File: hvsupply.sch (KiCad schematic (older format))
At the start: 30 parts, among them Q1 TIP50, Q2 IRF740, Q3 IRF740, Q4 IRF740, U1 LR8

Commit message: Beginning to look like a PCB.
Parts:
- removed C?: 1u, ~, symbol C
- removed K?: CONN_3, symbol CONN_3
- removed P?: CONN_2, symbol CONN_2
- added C3, C4, C5, C6, C7: .01, ~, symbol C
- added D5, D6: 16V, 1.3W, ~, symbol ZENER
- added K1: CONN_3, symbol CONN_3
- added P1, P2, P3, P4: CONN_2, symbol CONN_2
- added P10, P5, P6, P7, P8, P9: CONN_1, symbol CONN_1
- added Q2, Q3: IRF740, TO220, symbol IRF740
- added R10, R11: 16.2, 3W, ~, symbol R
- added R15: 10M, ~, symbol R
- added R16: 10k, ~, symbol R
- added R5, R6: 100, ~, symbol R
- gave numbers to parts that had none: 3
- renumbered D5 to D7, D6 to D8, D7 to D9, Q2 to Q4, Q3 to Q5, Q4 to Q6, R7 to R12, R8 to R13, R9 to R14, R1 to R2, R2 to R3, R3 to R4, R4 to R7, R5 to R8, R6 to R9
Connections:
- net GND: now also C3.1, C4.1, C5.1, C6.1, C7.1, P1.2 (PM), P10.1, P3.2 (PM), P4.2 (PM), P5.1, P6.1, P7.1, P8.1, P9.1, R16.2
- net HV_UNREG: now reaches C1.1, C2.1, D2.2 (K), D4.2 (K), Q4.1 (D), Q5.1 (D), Q6.1 (D), U1.1 (VIN)
- net HV_UNREG: now also Q2.1 (D), Q3.1 (D)
- net at D7.2 (K), Q4.2 (G), R7.2: now also C5.2
- net at D8.2 (K), Q5.2 (G), R8.2: now also C6.2
- net at D9.2 (K), Q6.2 (G), R9.2: now also C7.2
- net at R7.1, R8.1, R9.1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: now also R2.1, R5.1, R6.1
- net HV_OUT: now reaches R12.2, R13.2, R14.2
- net HV_OUT: now also P2.1 (P1), R10.2, R11.2, R15.1
- net SENSE_I: now reaches Q1.1 (B), R3.2, R4.1
- net SENSE_I: now also P2.2 (PM), P3.1 (P1)
- net HV_IN_LO: now reaches K2.1 (T1)
- net HV_IN_LO: now also K1.3 (P3)
- net HV_IN_HI: now reaches K2.14 (R2), K2.16 (T2)
- net HV_IN_HI: now also K1.1 (P1)
- net at K2.3 (R1): now also K1.2 (PM)
- net +12V renamed 12V_IN
- net 12V_IN: now also P1.1 (P1)
- new net: C4.2, D6.2 (K), Q3.2 (G), R6.2
- new net: D6.1 (A), Q3.3 (S), R11.1
- new net: C3.2, D5.2 (K), Q2.2 (G), R5.2
- new net: D5.1 (A), Q2.3 (S), R10.1
- new net SENSE_V: P4.1 (P1), R15.2, R16.1
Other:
- moved on the sheet: C1, C2, D1, D2, D3, D4, D7, D8, D9, K2, Q1, Q4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

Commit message: Fixed circuit error, added VCR for current limit adjustment, prototyping current limit indicator.
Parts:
- removed R4: 2.37, ~, symbol R
- added D?: LED, ~, symbol LED
- added Q?: MOSFET_N, ~, symbol MOSFET_N
- added Q?: PNP, ~, symbol PNP
- added R? (x3): R, ~, symbol R
- added RV?: POT, ~, symbol POT
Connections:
- net GND: now also Q?.S, R?.2, R?.2
- net SENSE_I: now also Q?.D, R?.1
- net at Q1.2 (C), U1.3 (ADJ): now also R2.2, RV1.2, RV1.3, Q?.2 (B)
- new net: Q?.G, R?.1, R?.2, RV?.3
- new net: D?.1 (A), Q?.3 (C)
- new net: D?.2 (K), R?.1
- new net +12V: Q?.1 (E), RV?.1, RV?.2
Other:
- note added: "Current Limit Indicator"
- note added: "Current Limit VCR"
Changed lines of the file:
@@
-EESchema Schematic File Version 2  date 7/6/2013 6:08:41 PM
+EESchema Schematic File Version 2  date 7/12/2013 8:46:22 PM
 LIBS:power
 LIBS:device
@@
 Sheet 1 1
 Title "Adjustable High Voltage Bench Supply"
-Date "7 jul 2013"
+Date "12 jul 2013"
 Rev ""
 Comp ""
@@
 $EndComp
 $Comp
-L R R4
-U 1 1 518B207E
-P 6350 5750
-F 0 "R4" V 6430 5750 40  0000 C CNN
-F 1 "2.37" V 6357 5751 40  0000 C CNN
-F 2 "~" V 6280 5750 30  0000 C CNN
-F 3 "~" H 6350 5750 30  0000 C CNN
-	1    6350 5750
-	1    0    0    -1
-$EndComp
-$Comp
 L CP1 C1
 U 1 1 518B20BA
@@
 F 3 "" H 4700 4550 60  0000 C CNN
 	1    4700 4550
-	1    0    0    -1
-$EndComp
-$Comp
-L GND #PWR03
-U 1 1 518B2146
-P 6350 6050
-F 0 "#PWR03" H 6350 6050 30  0001 C CNN
-F 1 "GND" H 6350 5980 30  0001 C CNN
-F 2 "" H 6350 6050 60  0000 C CNN
-F 3 "" H 6350 6050 60  0000 C CNN
-	1    6350 6050
 	1    0    0    -1
 $EndComp
@@
 	5000 2800 7850 2800
 Wire Wire Line
-	6350 5450 6350 5500
+	6350 5450 6350 6050
 Wire Wire Line
 	5900 5500 8600 5500
@@
 	3950 4350 3900 4350
 Connection ~ 3900 4350
-Wire Wire Line
-	6350 6000 6350 6050
 Wire Wire Line
 	7100 3350 7100 3400
@@
 Text Label 6750 2800 2    60   ~ 0
 HV_UNREG
+$Comp
+L MOSFET_N Q?
+U 1 1 51E03006
+P 6450 6250
+F 0 "Q?" H 6460 6420 60  0000 R CNN
+F 1 "MOSFET_N" H 6460 6100 60  0000 R CNN
+F 2 "~" H 6450 6250 60  0000 C CNN
+F 3 "~" H 6450 6250 60  0000 C CNN
+	1    6450 6250
+	-1   0    0    -1
+$EndComp
+$Comp
+L POT RV?
+U 1 1 51E0301C
+P 7250 6250
+F 0 "RV?" H 7250 6150 50  0000 C CNN
+F 1 "POT" H 7250 6250 50  0000 C CNN
+F 2 "~" H 7250 6250 60  0000 C CNN
+F 3 "~" H 7250 6250 60  0000 C CNN
+	1    7250 6250
+	-1   0    0    -1
+$EndComp
+$Comp
+L R R?
+U 1 1 51E03032
+P 6750 5900
+F 0 "R?" V 6830 5900 40  0000 C CNN
+F 1 "R" V 6757 5901 40  0000 C CNN
+F 2 "~" V 6680 5900 30  0000 C CNN
+F 3 "~" H 6750 5900 30  0000 C CNN
+	1    6750 5900
+	0    -1   -1   0
+$EndComp
+$Comp
+L R R?
+U 1 1 51E03041
+P 7000 6750
+F 0 "R?" V 7080 6750 40  0000 C CNN
+F 1 "R" V 7007 6751 40  0000 C CNN
+F 2 "~" V 6930 6750 30  0000 C CNN
+F 3 "~" H 7000 6750 30  0000 C CNN
+	1    7000 6750
+	1    0    0    -1
+$EndComp
+$Comp
+L PNP Q?
+U 1 1 51E03050
+P 5000 5200
+F 0 "Q?" H 5000 5050 60  0000 R CNN
+F 1 "PNP" H 5000 5350 60  0000 R CNN
+F 2 "~" H 5000 5200 60  0000 C CNN
+F 3 "~" H 5000 5200 60  0000 C CNN
+	1    5000 5200
+	-1   0    0    1
+$EndComp
+$Comp
+L LED D?
+U 1 1 51E03064
+P 4900 5800
+F 0 "D?" H 4900 5900 50  0000 C CNN
+F 1 "LED" H 4900 5700 50  0000 C CNN
+F 2 "~" H 4900 5800 60  0000 C CNN
+F 3 "~" H 4900 5800 60  0000 C CNN
+	1    4900 5800
+	0    1    1    0
+$EndComp
+$Comp
+L R R?
+U 1 1 51E03073
+P 4900 6350
+F 0 "R?" V 4980 6350 40  0000 C CNN
+F 1 "R" V 4907 6351 40  0000 C CNN
+F 2 "~" V 4830 6350 30  0000 C CNN
+F 3 "~" H 4900 6350 30  0000 C CNN
+	1    4900 6350
+	1    0    0    -1
+$EndComp
+$Comp
+L GND #PWR?
+U 1 1 51E03082
+P 4900 6800
+F 0 "#PWR?" H 4900 6800 30  0001 C CNN
+F 1 "GND" H 4900 6730 30  0001 C CNN
+F 2 "" H 4900 6800 60  0000 C CNN
+F 3 "" H 4900 6800 60  0000 C CNN
+	1    4900 6800
+	1    0    0    -1
+$EndComp
+$Comp
+L GND #PWR?
+U 1 1 51E03091
+P 6350 6700
+F 0 "#PWR?" H 6350 6700 30  0001 C CNN
+F 1 "GND" H 6350 6630 30  0001 C CNN
+F 2 "" H 6350 6700 60  0000 C CNN
+F 3 "" H 6350 6700 60  0000 C CNN
+	1    6350 6700
+	1    0    0    -1
+$EndComp
+$Comp
+L GND #PWR?
+U 1 1 51E030A0
+P 7000 7200
+F 0 "#PWR?" H 7000 7200 30  0001 C CNN
+F 1 "GND" H 7000 7130 30  0001 C CNN
+F 2 "" H 7000 7200 60  0000 C CNN
+F 3 "" H 7000 7200 60  0000 C CNN
+	1    7000 7200
+	1    0    0    -1
+$EndComp
+$Comp
+L +12V #PWR?
+U 1 1 51E030AF
+P 4900 4900
+F 0 "#PWR?" H 4900 4850 20  0001 C CNN
+F 1 "+12V" H 4900 5000 30  0000 C CNN
+F 2 "" H 4900 4900 60  0000 C CNN
+F 3 "" H 4900 4900 60  0000 C CNN
+	1    4900 4900
+	1    0    0    -1
+$EndComp
+Wire Wire Line
+	4900 4900 4900 5000
+Wire Wire Line
+	5200 5200 5600 5200
+Connection ~ 5600 5200
+Wire Wire Line
+	4900 5400 4900 5600
+Wire Wire Line
+	4900 6000 4900 6100
+Wire Wire Line
+	4900 6600 4900 6800
+Wire Wire Line
+	6350 5900 6500 5900
+Connection ~ 6350 5900
+Wire Wire Line
+	7000 5900 7000 6500
+Connection ~ 7000 6250
+Wire Wire Line
+	6650 6250 7000 6250
+Wire Wire Line
+	7250 6100 7500 6100
+Wire Wire Line
+	7500 5950 7500 6250
+$Comp
+L +12V #PWR?
+U 1 1 51E035F9
+P 7500 5950
+F 0 "#PWR?" H 7500 5900 20  0001 C CNN
+F 1 "+12V" H 7500 6050 30  0000 C CNN
+F 2 "" H 7500 5950 60  0000 C CNN
+F 3 "" H 7500 5950 60  0000 C CNN
+	1    7500 5950
+	1    0    0    -1
+$EndComp
+Connection ~ 7500 6100
+Wire Wire Line
+	7000 7000 7000 7200
+Wire Wire Line
+	6350 6450 6350 6700
+Text Notes 4700 6400 1    60   ~ 0
+Current Limit Indicator
+Text Notes 6250 6650 1    60   ~ 0
+Current Limit VCR
+Wire Wire Line
+	5600 4350 6350 4350
 $EndSCHEMATC

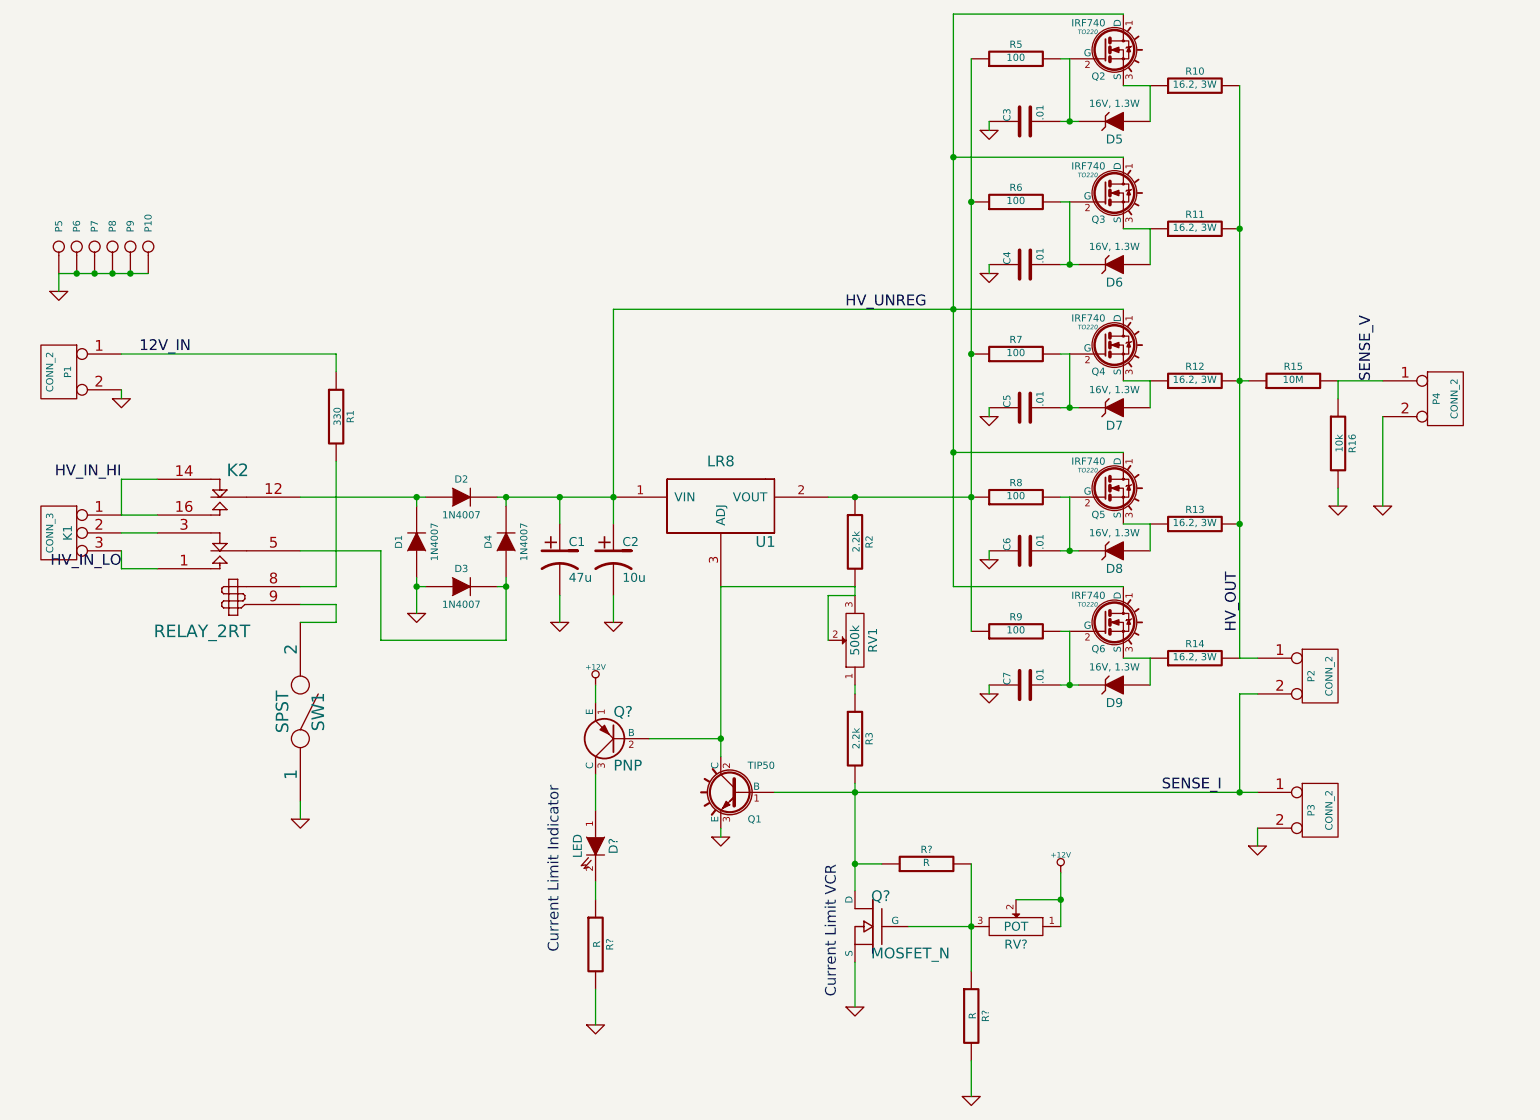
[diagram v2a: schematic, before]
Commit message: Major changes: unity-gain op-amps for current limit triggering and current sense buffering; comparator-based current limit indicator; voltage-controlled resistor-based adjustable current limit.
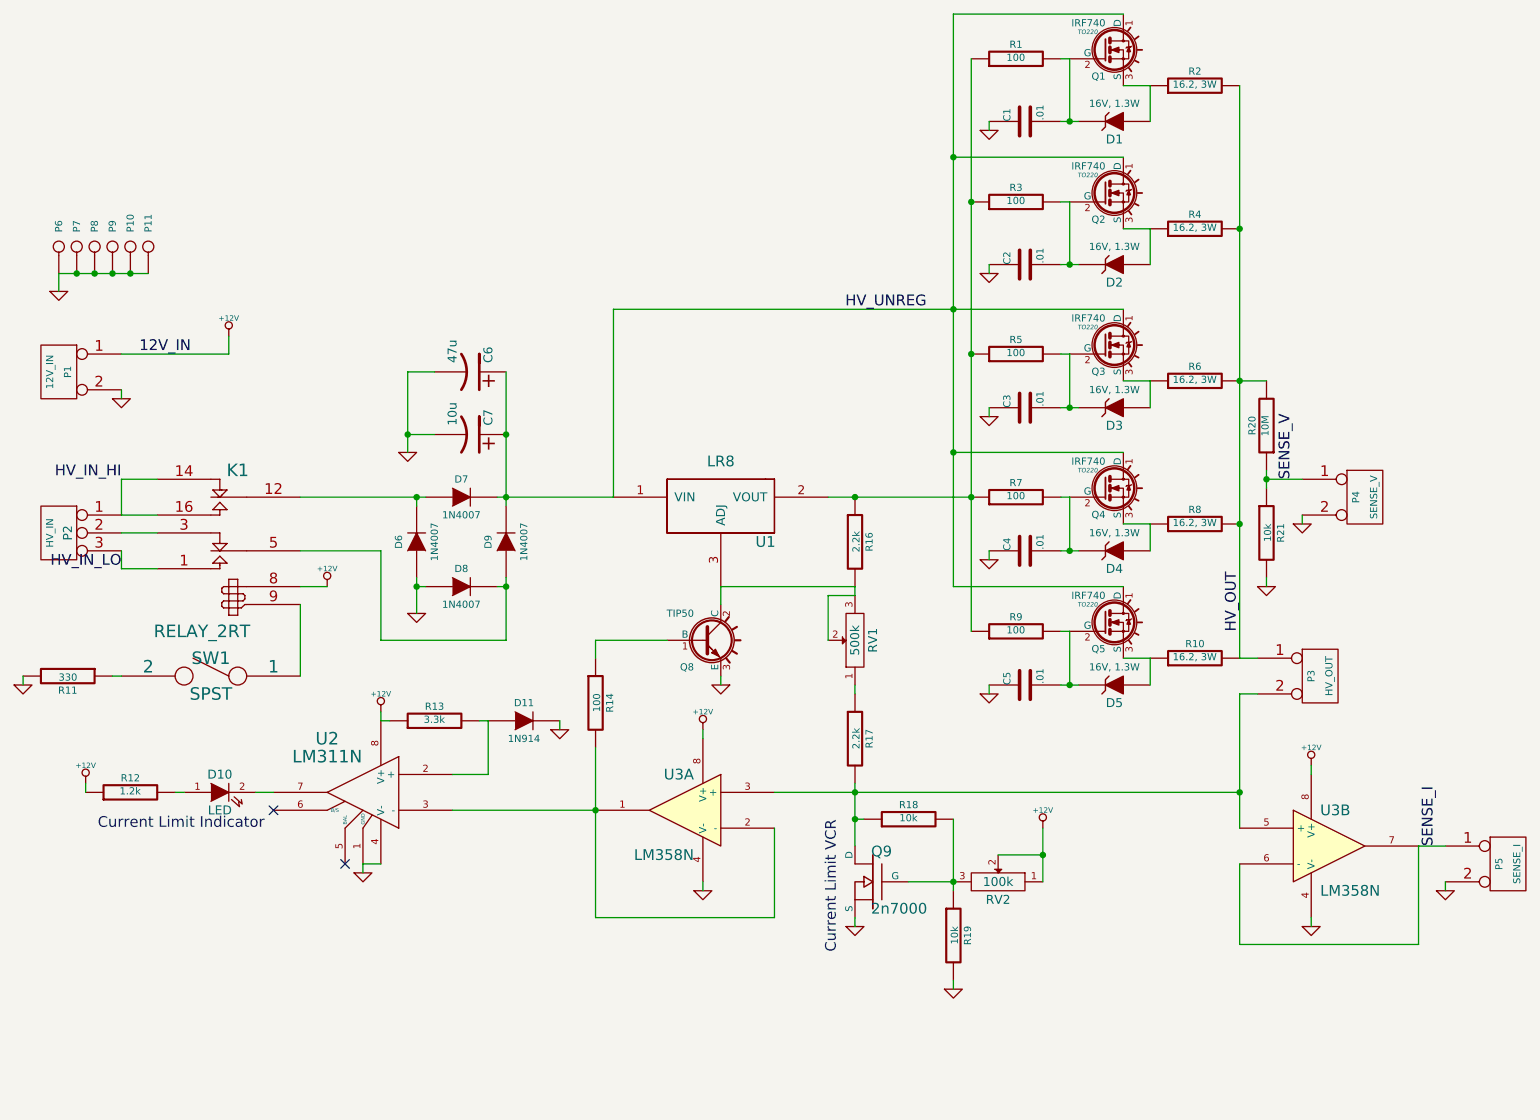
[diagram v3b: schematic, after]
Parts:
- removed Q?: PNP, ~, symbol PNP
- added D11: 1N914, symbol DIODE
- added R13: 3.3k, symbol R
- added R14: 100, symbol R
- added U2: LM311N, symbol LM311N
- added U3: LM358N, symbol LM358N
- P1: value CONN_2 -> 12V_IN
- P2: renamed from K1; value CONN_3 -> HV_IN
- P3: renamed from P2; value CONN_2 -> HV_OUT
- P4: value CONN_2 -> SENSE_V
- P5: renamed from P3; value CONN_2 -> SENSE_I
- Q9: renamed from Q?; value MOSFET_N -> 2n7000
- R12: renamed from R?; value R -> 1.2k
- R18, R19: renamed from R?; value R -> 10k
- RV2: renamed from RV?; value POT -> 100k
- gave numbers to parts that had none: 1
- renumbered C3 to C1, C4 to C2, C5 to C3, C6 to C4, C7 to C5, C1 to C6, C2 to C7, D5 to D1, D6 to D2, D7 to D3, D8 to D4, D9 to D5, D1 to D6, D2 to D7, D3 to D8, D4 to D9, K2 to K1, P9 to P10, P10 to P11, P5 to P6, P6 to P7, P7 to P8, P8 to P9, Q2 to Q1, Q3 to Q2, Q4 to Q3, Q5 to Q4, Q6 to Q5, Q1 to Q8, R5 to R1, R14 to R10, R1 to R11, R2 to R16, R3 to R17, R10 to R2, R15 to R20, R16 to R21, R6 to R3, R11 to R4, R7 to R5, R12 to R6, R8 to R7, R13 to R8
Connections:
- net +12V: now also K1.8, P1.1 (P1), R12.1, R13.1, U2.8 (V+), U3.8 (V+), U3.8 (V+)
- net GND: now also R11.2, D11.2 (K), U2.1 (GND), U2.4 (V-), U3.4 (V-), U3.4 (V-); no longer R12.2, SW1.1
- net HV_OUT: now also R20.2; no longer R20.1
- net SENSE_I: now also U3.6 (-), U3.7; no longer P3.2 (PM), Q8.1 (B), Q9.D, R17.2, R18.1
- net SENSE_V: now also R20.1; no longer R20.2
- net at K1.9: now also SW1.1; no longer SW1.2
- net at D10.1 (A): now also R12.2
- net at D10.2 (K): now also U2.7; no longer R12.1
- net 12V_IN: no longer names the net of R11.1
- net 12V_IN: now also SW1.2; no longer P1.1 (P1)
- new net: P3.2 (PM), Q9.D, R17.2, R18.1, U3.3 (+), U3.5 (+)
- new net: Q8.1 (B), R14.1
- new net: D11.1 (A), R13.2, U2.2 (+)
- new net: R14.2, U2.3 (-), U3.1, U3.2 (-)
- no-connect marks 0 -> 2
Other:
- moved on the sheet: C6, C7, D10, P4, P5, Q8, Q9, R11, R12, R18, R19, R20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

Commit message: Started from scratch on the PCB.  Parts placement mostly done.
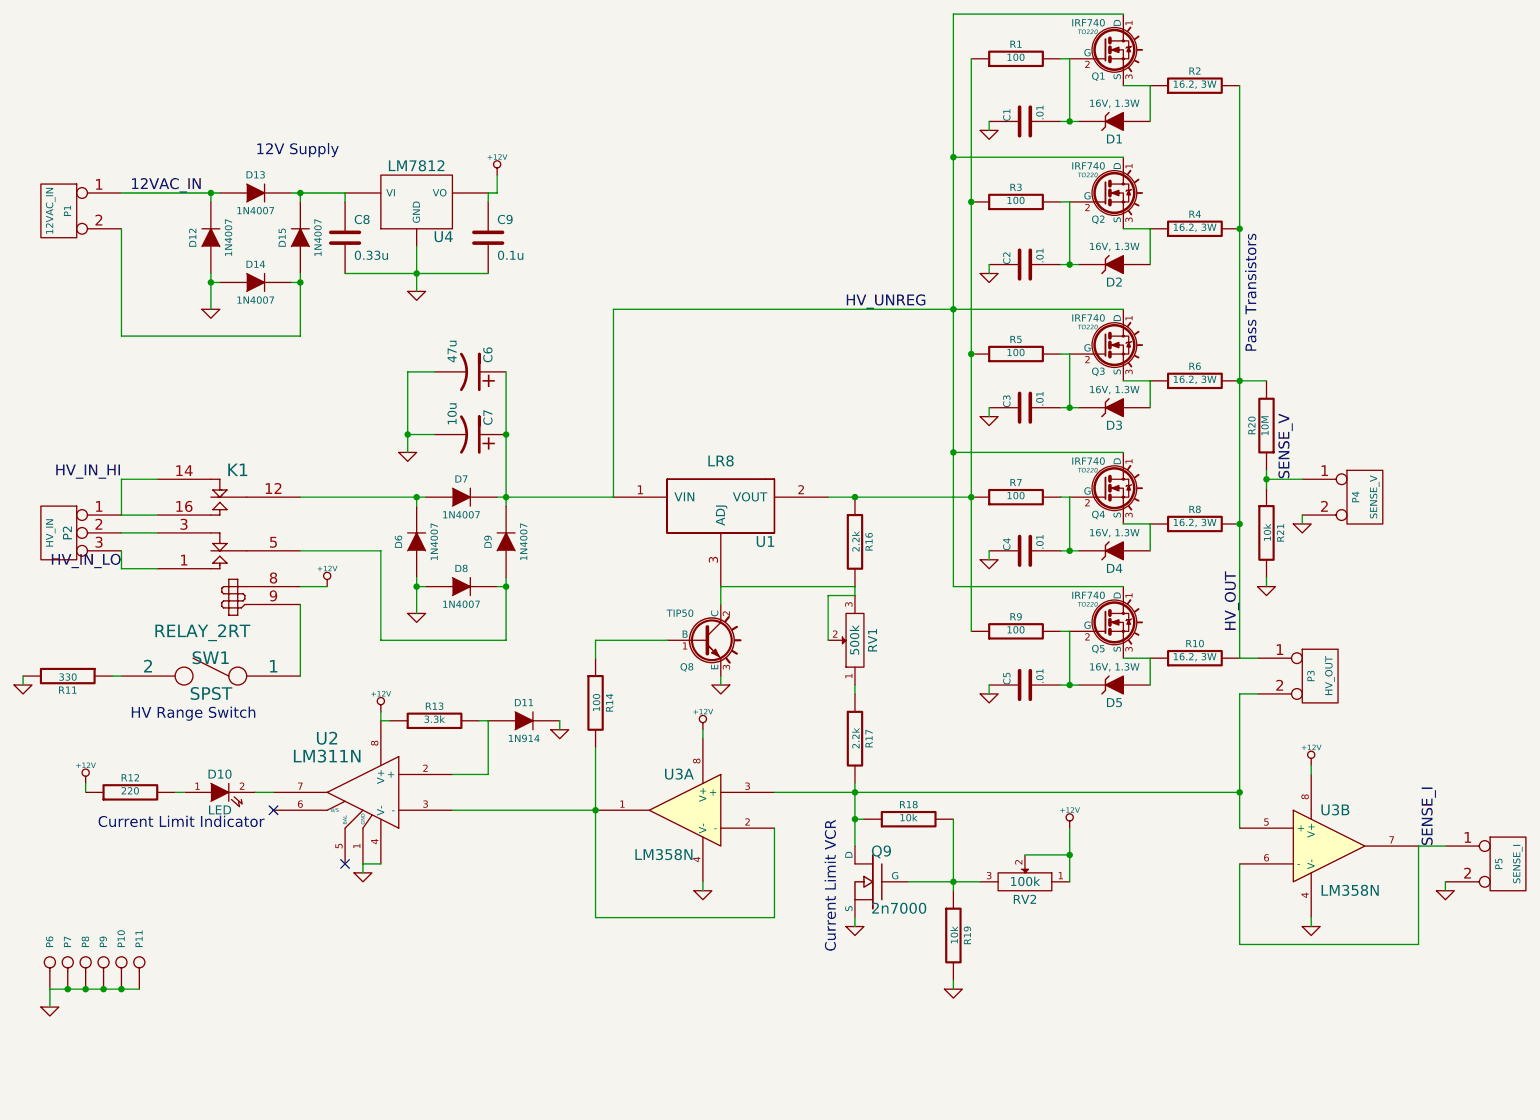
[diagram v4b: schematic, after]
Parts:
- added C8: 0.33u, symbol C
- added C9: 0.1u, symbol C
- added D12, D13, D14, D15: 1N4007, symbol DIODE
- added U4: LM7812, symbol LM7812
- P1: value 12V_IN -> 12VAC_IN
- R12: value 1.2k -> 220
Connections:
- net +12V: now also C9.1, U4.VO; no longer P1.1 (P1)
- net GND: now also C8.2, C9.2, D12.1 (A), D14.1 (A), U4.GND; no longer P1.2 (PM)
- new net: D14.2 (K), D15.1 (A), P1.2 (PM)
- new net: C8.1, D13.2 (K), D15.2 (K), U4.VI
- new net 12VAC_IN: D12.2 (K), D13.1 (A), P1.1 (P1)
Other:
- note added: "12V Supply"
- note added: "HV Range Switch"
- note added: "Pass Transistors"
- moved on the sheet: P1, P10, P11, P6, P7, P8, P9, RV2
